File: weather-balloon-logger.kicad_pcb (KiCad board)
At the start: 2 copper layers, 80 x 78.5 mm, 24 parts, among them J1 Conn_01x02, J2 Conn_01x11, J3 SMA, J4 SMA, J5 Conn_01x02, J6 VHF, J7 HF, Q1 AO3400A, SW1 SPDT, U1 PCF8574T

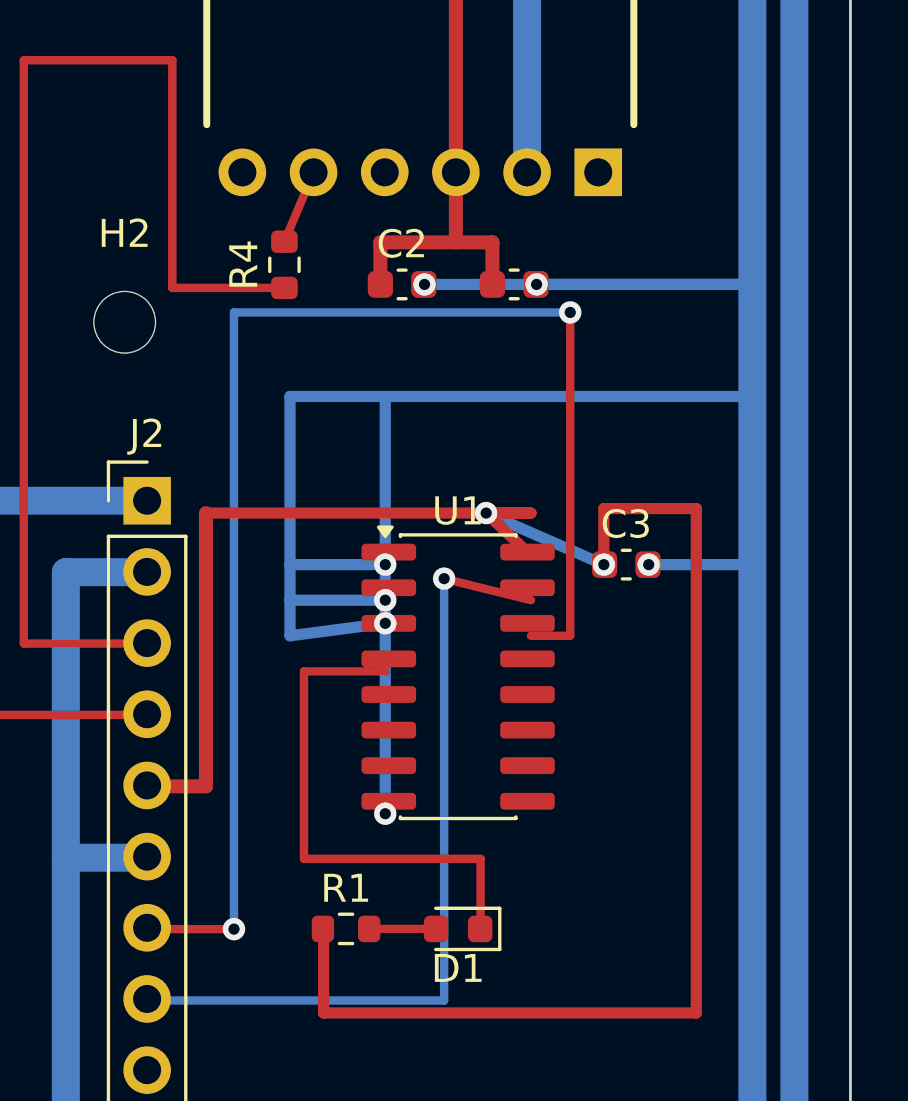
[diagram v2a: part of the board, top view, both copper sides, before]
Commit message: fix(pcb): make R4 through-hole
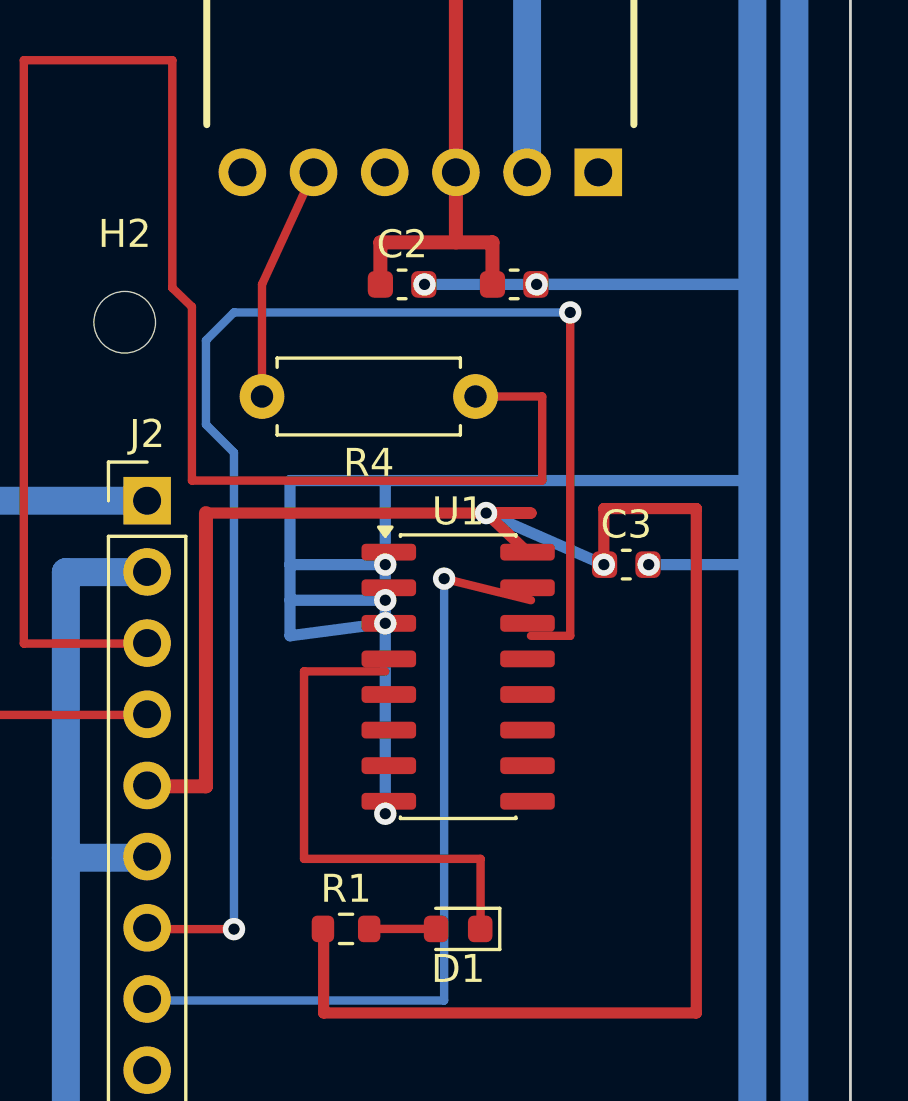
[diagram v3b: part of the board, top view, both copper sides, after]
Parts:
- R4: footprint R_0603_1608Metric -> R_Axial_DIN0207_L6.3mm_D2.5mm_P7.62mm_Horizontal
- moved R4 8.28 mm to (166.6, 118.0), turned to 180 degrees
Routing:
- net UART_TX: track 42.6 -> 63.7 mm
- net GND: track 517.3 -> 511.3 mm
- net OPENLOG_RXI: track 2.68 -> 8.40 mm
- net I2C_SCL: track 50.0 -> 50.9 mm
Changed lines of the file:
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@@
 		(embedded_fonts no)
 	)
-	(footprint "R_0603_1608Metric"
-		(layer "F.Cu")
-		(at 159.8 113.3 90)
-		(descr "Resistor SMD 0603 (1608 Metric), square (rectangular) end terminal, IPC-7351 nominal")
-		(tags "resistor")
-		(property "Reference" "R4" (at 0 -1.43 270) (layer "F.SilkS") (effects (font (size 1 1) (thickness 0.15))))
-		(property "Value" "1k" (at 0 1.43 270) (layer "F.Fab") (effects (font (size 1 1) (thickness 0.15))))
-		(property "Datasheet" "" (at 0 0 270) (layer "F.Fab") (hide yes) (effects (font (size 1.27 1.27))))
-		(property "Description" "" (at 0 0 270) (layer "F.Fab") (hide yes) (effects (font (size 1.27 1.27))))
-		(attr smd board_only)
+	(footprint "R_Axial_DIN0207_L6.3mm_D2.5mm_P7.62mm_Horizontal"
+		(layer "F.Cu")
+		(at 166.62 118 180)
+		(descr "Resistor, Axial_DIN0207 series, Axial, Horizontal, pin pitch=7.62mm, 0.25W = 1/4W, length*diameter=6.3*2.5mm^2")
+		(tags "Resistor Axial DIN0207 THT 1/4W")
+		(property "Reference" "R4" (at 3.81 -2.37 0) (layer "F.SilkS") (effects (font (size 1 1) (thickness 0.15))))
+		(property "Value" "1k" (at 3.81 2.37 0) (layer "F.Fab") (effects (font (size 1 1) (thickness 0.15))))
+		(property "Datasheet" "" (at 0 0 180) (layer "F.Fab") (hide yes) (effects (font (size 1.27 1.27))))
+		(property "Description" "1 kOhm 1/4 W axial through-hole resistor" (at 0 0 180) (layer "F.Fab") (hide yes) (effects (font (size 1.27 1.27))))
+		(attr through_hole board_only)
 		(duplicate_pad_numbers_are_jumpers no)
-		(fp_line (start -0.237258 -0.5225) (end 0.237258 -0.5225) (stroke (width 0.12) (type solid)) (layer "F.SilkS"))
-		(fp_line (start -0.237258 0.5225) (end 0.237258 0.5225) (stroke (width 0.12) (type solid)) (layer "F.SilkS"))
-		(fp_rect (start -1.48 -0.73) (end 1.48 0.73) (stroke (width 0.05) (type solid)) (fill no) (layer "F.CrtYd"))
-		(fp_rect (start -0.8 -0.4125) (end 0.8 0.4125) (stroke (width 0.1) (type solid)) (fill no) (layer "F.Fab"))
-		(fp_text user "${REFERENCE}" (at 0 0 270) (layer "F.Fab") (effects (font (size 0.4 0.4) (thickness 0.06))))
-		(pad "1" smd roundrect (at -0.825 0 270) (size 0.8 0.95) (layers "F.Cu" "F.Mask" "F.Paste") (roundrect_rratio 0.25) (net "UART_TX"))
-		(pad "2" smd roundrect (at 0.825 0 270) (size 0.8 0.95) (layers "F.Cu" "F.Mask" "F.Paste") (roundrect_rratio 0.25) (net "OPENLOG_RXI"))
+		(fp_line (start 0.54 -1.37) (end 7.08 -1.37) (stroke (width 0.12) (type solid)) (layer "F.SilkS"))
+		(fp_line (start 0.54 -1.04) (end 0.54 -1.37) (stroke (width 0.12) (type solid)) (layer "F.SilkS"))
+		(fp_line (start 0.54 1.04) (end 0.54 1.37) (stroke (width 0.12) (type solid)) (layer "F.SilkS"))
+		(fp_line (start 0.54 1.37) (end 7.08 1.37) (stroke (width 0.12) (type solid)) (layer "F.SilkS"))
+		(fp_line (start 7.08 -1.37) (end 7.08 -1.04) (stroke (width 0.12) (type solid)) (layer "F.SilkS"))
+		(fp_line (start 7.08 1.37) (end 7.08 1.04) (stroke (width 0.12) (type solid)) (layer "F.SilkS"))
+		(fp_rect (start -1.05 -1.5) (end 8.67 1.5) (stroke (width 0.05) (type solid)) (fill no) (layer "F.CrtYd"))
+		(fp_line (start 0 0) (end 0.66 0) (stroke (width 0.1) (type solid)) (layer "F.Fab"))
+		(fp_line (start 7.62 0) (end 6.96 0) (stroke (width 0.1) (type solid)) (layer "F.Fab"))
+		(fp_rect (start 0.66 -1.25) (end 6.96 1.25) (stroke (width 0.1) (type solid)) (fill no) (layer "F.Fab"))
+		(fp_text user "${REFERENCE}" (at 3.81 0 0) (layer "F.Fab") (effects (font (size 1 1) (thickness 0.15))))
+		(pad "1" thru_hole circle (at 0 0 180) (size 1.6 1.6) (drill 0.8) (layers "*.Cu" "*.Mask") (remove_unused_layers no) (net "UART_TX"))
+		(pad "2" thru_hole circle (at 7.62 0 180) (size 1.6 1.6) (drill 0.8) (layers "*.Cu" "*.Mask") (remove_unused_layers no) (net "OPENLOG_RXI"))
 		(embedded_fonts no)
-		(model "${KICAD10_3DMODEL_DIR}/Resistor_SMD.3dshapes/R_0603_1608Metric.step" (offset (xyz 0 0 0)) (scale (xyz 1 1 1)) (rotate (xyz 0 0 0)))
+		(model "${KICAD10_3DMODEL_DIR}/Resistor_THT.3dshapes/R_Axial_DIN0207_L6.3mm_D2.5mm_P7.62mm_Horizontal.step" (offset (xyz 0 0 0)) (scale (xyz 1 1 1)) (rotate (xyz 0 0 0)))
 	)
 	(gr_text "JAVAS Logger"
@@
 	(segment
 		(start 160 124)
-		(end 160 118)
-		(width 0.4)
-		(layer "B.Cu")
-		(net "GND")
-	)
-	(segment
-		(start 160 118)
-		(end 176.5 118)
+		(end 160 121)
+		(width 0.4)
+		(layer "B.Cu")
+		(net "GND")
+	)
+	(segment
+		(start 160 121)
+		(end 176.5 121)
 		(width 0.4)
 		(layer "B.Cu")
@@
 	(segment
 		(start 163.4 132.89)
-		(end 163.4 118)
+		(end 163.4 121)
 		(width 0.4)
 		(layer "B.Cu")
@@
 		(net "I2C_SCL")
 	)
-	(segment
-		(start 158 137.008)
-		(end 158 115)
-		(width 0.3)
-		(layer "B.Cu")
-		(net "I2C_SCL")
-	)
+	(segment (start 158 137.008) (end 158 120) (width 0.3) (layer "B.Cu") (net "I2C_SCL"))
+	(segment (start 158 120) (end 157 119) (width 0.3) (layer "B.Cu") (net "I2C_SCL"))
+	(segment (start 157 119) (end 157 116) (width 0.3) (layer "B.Cu") (net "I2C_SCL"))
+	(segment (start 157 116) (end 158 115) (width 0.3) (layer "B.Cu") (net "I2C_SCL"))
 	(segment
 		(start 158 115)
@@
 		(net "UART_TX")
 	)
-	(segment (start 155.8 114.125) (end 159.8 114.125) (width 0.3) (layer "F.Cu") (net "UART_TX"))
-	(segment (start 159.8 112.475) (end 160.84 110) (width 0.3) (layer "F.Cu") (net "OPENLOG_RXI"))
+	(segment (start 155.8 114.125) (end 156.5 114.8) (width 0.3) (layer "F.Cu") (net "UART_TX"))
+	(segment (start 156.5 114.8) (end 156.5 121) (width 0.3) (layer "F.Cu") (net "UART_TX"))
+	(segment (start 156.5 121) (end 169 121) (width 0.3) (layer "F.Cu") (net "UART_TX"))
+	(segment (start 169 121) (end 169 118) (width 0.3) (layer "F.Cu") (net "UART_TX"))
+	(segment (start 169 118) (end 166.62 118) (width 0.3) (layer "F.Cu") (net "UART_TX"))
+	(segment (start 159 118) (end 159 114) (width 0.3) (layer "F.Cu") (net "OPENLOG_RXI"))
+	(segment (start 159 114) (end 160.84 110) (width 0.3) (layer "F.Cu") (net "OPENLOG_RXI"))
 	(segment
 		(start 154.9 129.364)

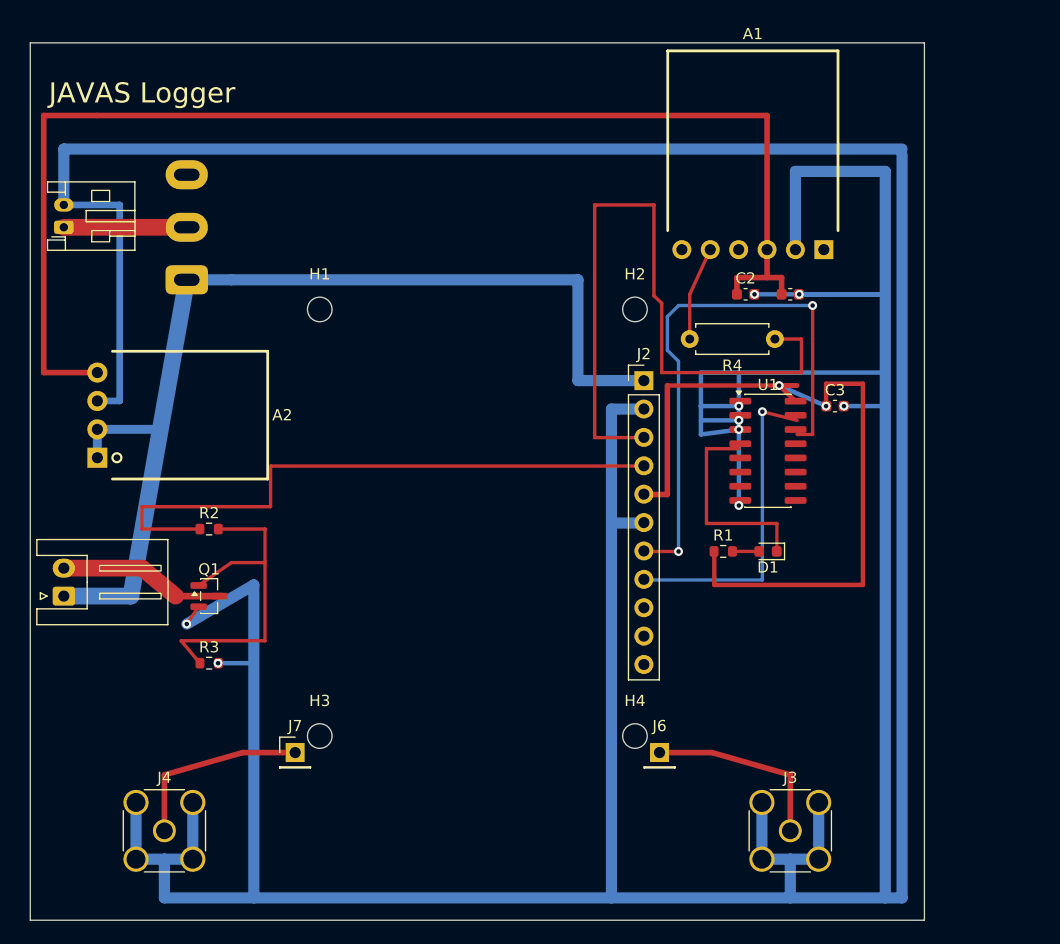
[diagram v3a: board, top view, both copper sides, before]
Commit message: copperhead: Final PCB mechanical/legend cleanup. Current electrical DRC is clean with zero unconnected pads. Do not change schematic, intent, BOM, scripts, outline, RF routes, or functional topology. Fix the remaining 30 DRC findings only: move C4 and C5 to eliminate both J5 courtyard overlaps and three PTH-inside-courtyard errors, rerouting only their LOGGER_5V/GND connections while preserving electrical cleanliness; adjust F.SilkS geometry in both project KEMET footprint library files and their embedded C1-C5 board footprints so silk does not cross their own pad solder-mask openings; reposition or hide only reference text and local silk strokes causing the listed U1/R4, J5/C4/C5, U2/R3/Q1, and A2/U2 silk collisions. Preserve fabrication/fab/courtyard dimensions and all pads. Finish with normal KiCad DRC zero violations and zero unconnected items. Do not commit.
Completed the bounded PCB mechanical/legend cleanup without committing. Moved C4 to (107.7,133.3) and C5 to (103,115.5), rerouted only their LOGGER_5V/GND connections, converted both project KEMET footprint silks and all embedded C1-C5 copies to pad-clear strokes, and hid only the identified colliding reference fields. Pads, courtyards, fab geometry, outline, RF routes, schematic, intent, BOM, scripts, and functional topology were preserved. Normal KiCad DRC is clean with zero violations and zero unconnected items; ERC is clean; schematic legibility has no findings; PINOUT drift was reconciled to the unchanged captured cutdown-driver topology.

Verification: ERC clean, DRC clean
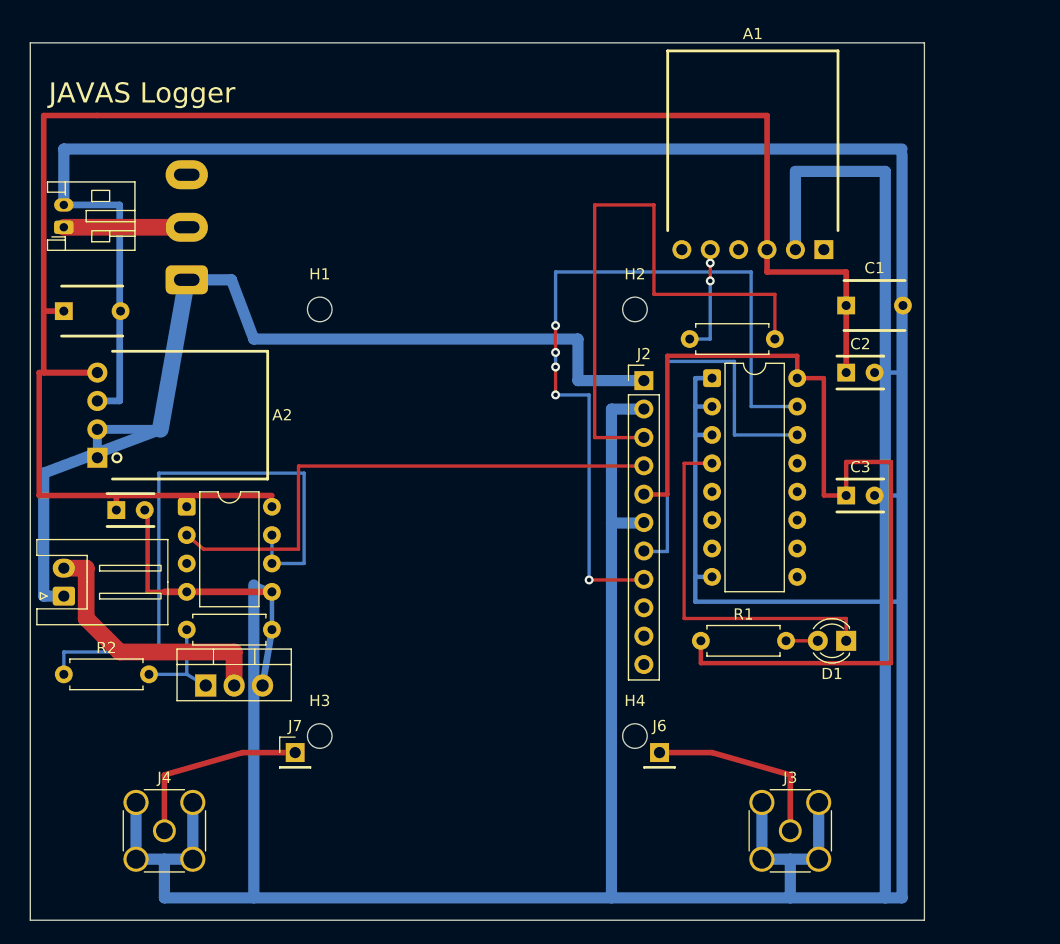
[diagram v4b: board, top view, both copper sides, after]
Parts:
- added C4: 100nF, KEMET_C315C104K5R5TA, F.Cu at (107.7, 133.3)
- added C5: 4.7uF, KEMET_C322C475K5R5TA, F.Cu at (103.0, 115.5)
- added U2: TC4422AVPA, DIP-8_W7.62mm, F.Cu at (114.0, 133.0)
- C1: footprint C_0603_1608Metric -> KEMET_C322C475K5R5TA
- C2, C3: footprint C_0603_1608Metric -> KEMET_C315C104K5R5TA
- D1: footprint LED_0603_1608Metric -> LED_D3.0mm
- Q1: footprint SOT-23 -> TO-220-3_Vertical
- R1, R2, R3: footprint R_0603_1608Metric -> R_Axial_DIN0207_L6.3mm_D2.5mm_P7.62mm_Horizontal
- U1: footprint SOIC-16_3.9x9.9mm_P1.27mm -> DIP-16_W7.62mm
- moved R2 18.4 mm to (103.0, 148.0)
- moved C2 11.4 mm to (173.0, 121.0)
- moved D1 10.6 mm to (173.0, 145.0)
- moved R1 8.25 mm to (160.0, 145.0)
- moved U1 8.20 mm to (161.0, 121.5)
- moved C3 8.06 mm to (173.0, 132.0)
- moved Q1 8.01 mm to (115.7, 149.0)
- moved C1 5.10 mm to (173.0, 115.0)
- moved R3 3.61 mm to (114.0, 144.0)
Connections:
- Q1 pad 2: GND -> CUTDOWN_DRAIN
- Q1 pad 3: CUTDOWN_DRAIN -> GND
- R2 pad 1: CUTDOWN_CTRL -> CUTDOWN_DRIVE
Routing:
- net CUTDOWN_DRIVE: track 0.00 -> 53.0 mm
- net LOGGER_5V: track 114.0 -> 162.7 mm
- net I2C_SDA: track 28.9 -> 69.1 mm, vias 1 -> 5
- net CUTDOWN_GATE: track 30.9 -> 9.35 mm
- net 3V3: track 71.3 -> 87.0 mm, vias 2 -> 0
- net LED_N: track 18.4 -> 32.9 mm
- net I2C_SCL: track 50.9 -> 37.3 mm, vias 2 -> 0
- net UART_TX: track 63.7 -> 53.3 mm
- net CUTDOWN_DRAIN: track 15.0 -> 24.0 mm
- net CUTDOWN_CTRL: track 55.7 -> 48.8 mm
- net OPENLOG_RXI: track 8.40 -> 9.84 mm, vias 0 -> 2
- net GND: track 511.3 -> 512.5 mm, vias 9 -> 0
- net PACK_SW: track 92.8 -> 94.0 mm

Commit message: feat(pcb): add functional silkscreen labels
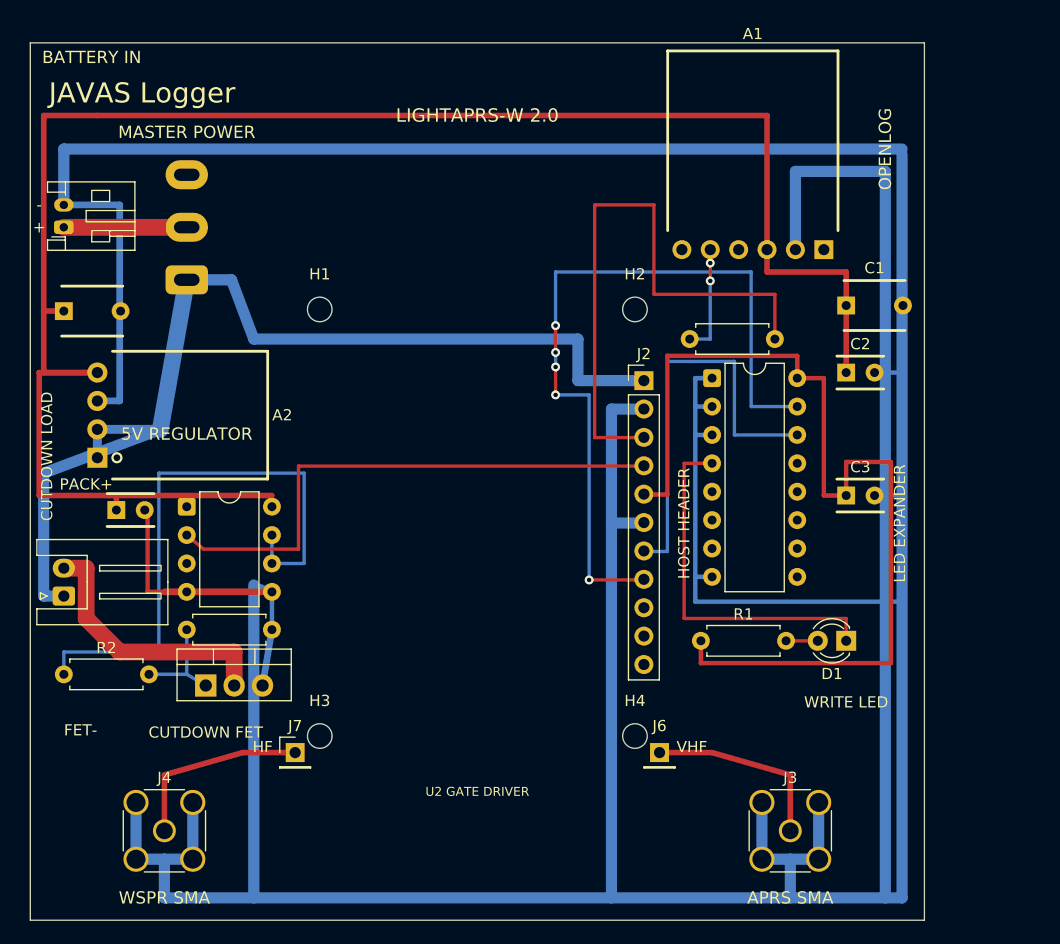
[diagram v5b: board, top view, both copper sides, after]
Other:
- board text added: "+"
- board text added: "-"
- board text added: "5V REGULATOR"
- board text added: "APRS SMA"
- board text added: "BATTERY IN"
- board text added: "CUTDOWN FET"
- board text added: "CUTDOWN LOAD"
- board text added: "FET-"
- board text added: "HF"
- board text added: "HOST HEADER"
- board text added: "LED EXPANDER"
- board text added: "LIGHTAPRS-W 2.0"
- board text added: "MASTER POWER"
- board text added: "OPENLOG"
- board text added: "PACK+"
- board text added: "U2 GATE DRIVER"
- board text added: "VHF"
- board text added: "WRITE LED"
- board text added: "WSPR SMA"
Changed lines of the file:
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@@
 		)
+	)
+	(gr_text "BATTERY IN"
+		(at 105.5 92.8 0)
+		(layer "F.SilkS")
+		(effects (font (size 1.1 1.1) (thickness 0.18)))
+	)
+	(gr_text "+"
+		(at 100.8 108 0)
+		(layer "F.SilkS")
+		(effects (font (size 1 1) (thickness 0.18)))
+	)
+	(gr_text "-"
+		(at 100.8 106 0)
+		(layer "F.SilkS")
+		(effects (font (size 1 1) (thickness 0.18)))
+	)
+	(gr_text "MASTER POWER"
+		(at 114 99.5 0)
+		(layer "F.SilkS")
+		(effects (font (size 1.1 1.1) (thickness 0.18)))
+	)
+	(gr_text "5V REGULATOR"
+		(at 114 126.5 0)
+		(layer "F.SilkS")
+		(effects (font (size 1.1 1.1) (thickness 0.18)))
+	)
+	(gr_text "OPENLOG"
+		(at 176.5 101 90)
+		(layer "F.SilkS")
+		(effects (font (size 1.1 1.1) (thickness 0.18)))
+	)
+	(gr_text "LIGHTAPRS-W 2.0"
+		(at 140 98 0)
+		(layer "F.SilkS")
+		(effects (font (size 1.2 1.2) (thickness 0.2)))
+	)
+	(gr_text "HOST HEADER"
+		(at 158.5 134.5 90)
+		(layer "F.SilkS")
+		(effects (font (size 1 1) (thickness 0.18)))
+	)
+	(gr_text "LED EXPANDER"
+		(at 177.8 134.5 90)
+		(layer "F.SilkS")
+		(effects (font (size 1 1) (thickness 0.18)))
+	)
+	(gr_text "U2 GATE DRIVER"
+		(at 140 158.5 0)
+		(layer "F.SilkS")
+		(effects (font (size 0.8 0.8) (thickness 0.15)))
+	)
+	(gr_text "CUTDOWN LOAD"
+		(at 101.5 128.5 90)
+		(layer "F.SilkS")
+		(effects (font (size 1 1) (thickness 0.18)))
+	)
+	(gr_text "PACK+"
+		(at 105 131 0)
+		(layer "F.SilkS")
+		(effects (font (size 1 1) (thickness 0.18)))
+	)
+	(gr_text "FET-"
+		(at 104.5 153 0)
+		(layer "F.SilkS")
+		(effects (font (size 1 1) (thickness 0.18)))
+	)
+	(gr_text "CUTDOWN FET"
+		(at 115.7 153.2 0)
+		(layer "F.SilkS")
+		(effects (font (size 1 1) (thickness 0.18)))
+	)
+	(gr_text "WRITE LED"
+		(at 173 150.5 0)
+		(layer "F.SilkS")
+		(effects (font (size 1 1) (thickness 0.18)))
+	)
+	(gr_text "VHF"
+		(at 159.2 154.5 0)
+		(layer "F.SilkS")
+		(effects (font (size 1 1) (thickness 0.18)))
+	)
+	(gr_text "HF"
+		(at 120.8 154.5 0)
+		(layer "F.SilkS")
+		(effects (font (size 1 1) (thickness 0.18)))
+	)
+	(gr_text "APRS SMA"
+		(at 168 168 0)
+		(layer "F.SilkS")
+		(effects (font (size 1.1 1.1) (thickness 0.18)))
+	)
+	(gr_text "WSPR SMA"
+		(at 112 168 0)
+		(layer "F.SilkS")
+		(effects (font (size 1.1 1.1) (thickness 0.18)))
 	)
 	(segment
